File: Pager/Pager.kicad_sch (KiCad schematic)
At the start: 28 parts, among them J1 Conn_01x02_Pin, SW7 SW_Push, SW8 SW_Push, U1 ESP32-S3-MINI-1

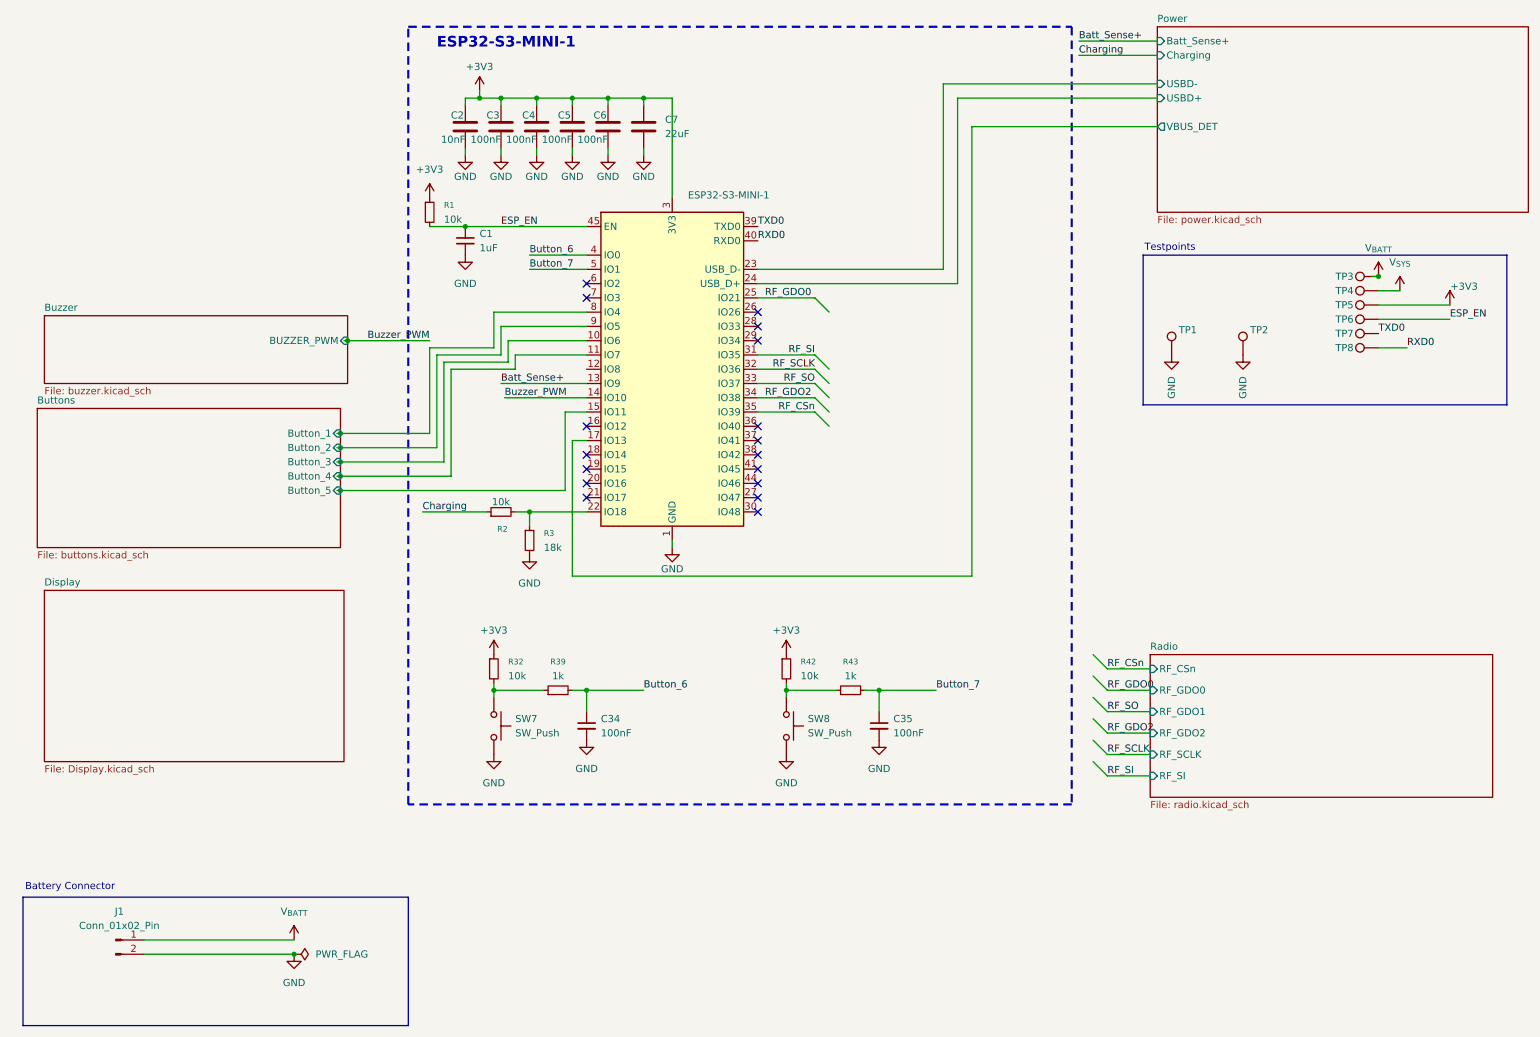
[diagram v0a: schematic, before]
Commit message: add display module
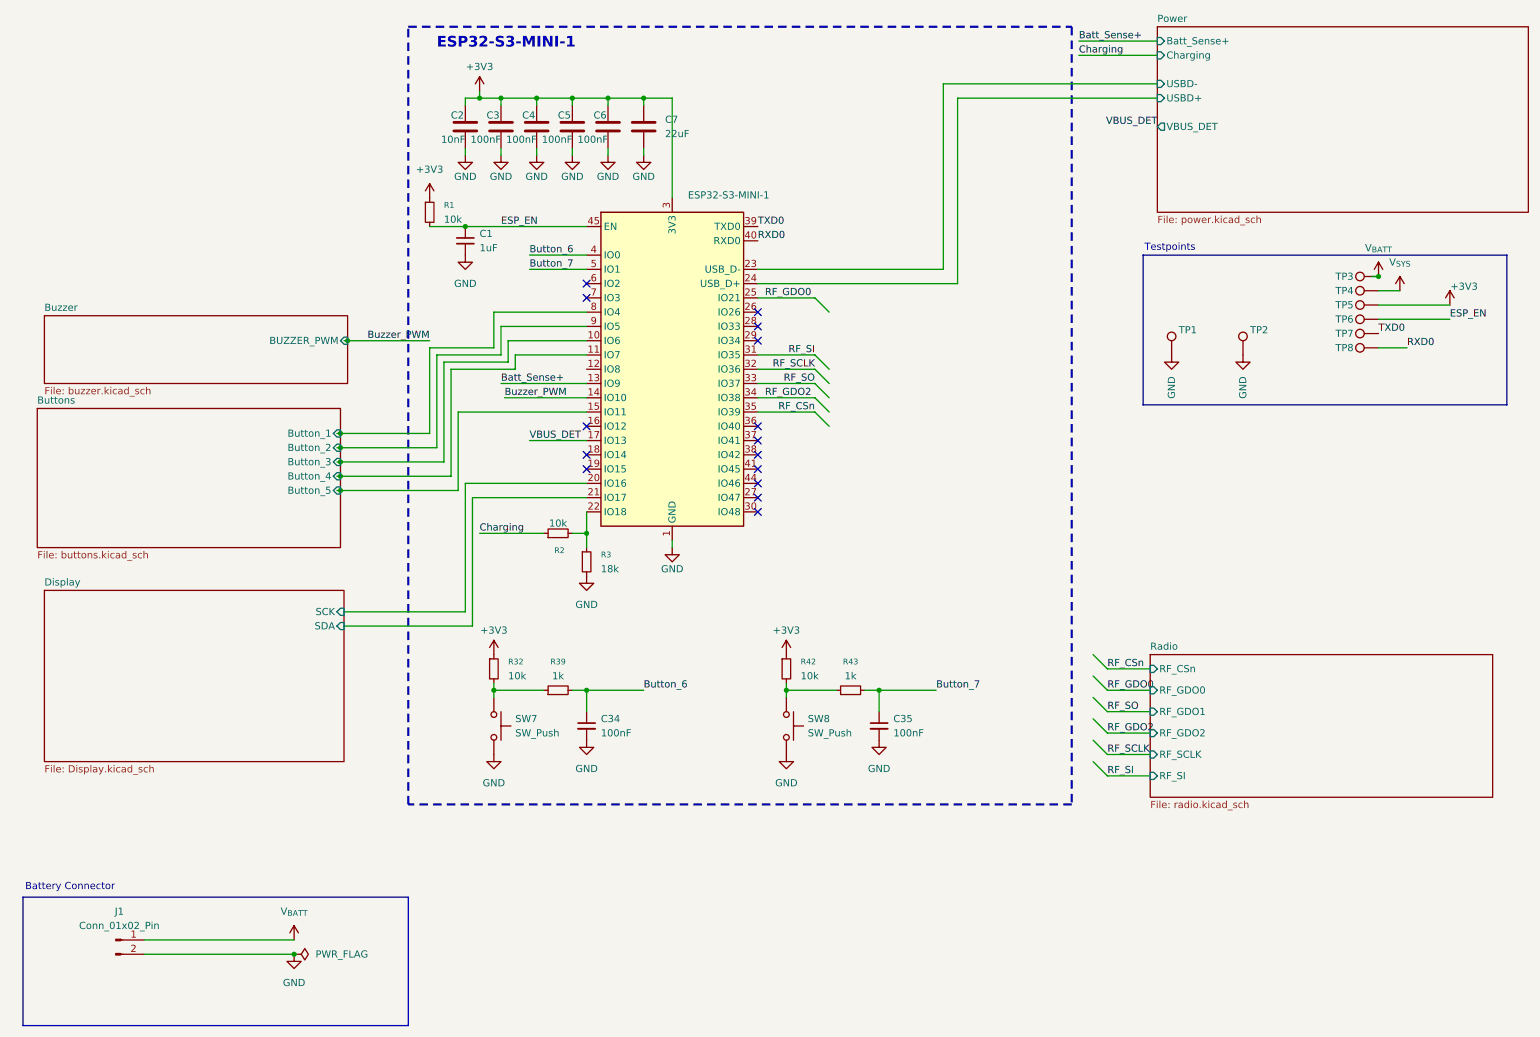
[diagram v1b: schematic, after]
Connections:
- net Display/SCK: now reaches U1.20 (IO16)
- net Display/SDA: now reaches U1.21 (IO17)
- net Power/VBUS_DET renamed VBUS_DET
- no-connect marks 17 -> 15
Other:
- sheet Display ports: added SCK, SDA; removed none
- moved on the sheet: R2, R3
